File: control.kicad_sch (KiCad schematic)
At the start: 0 parts

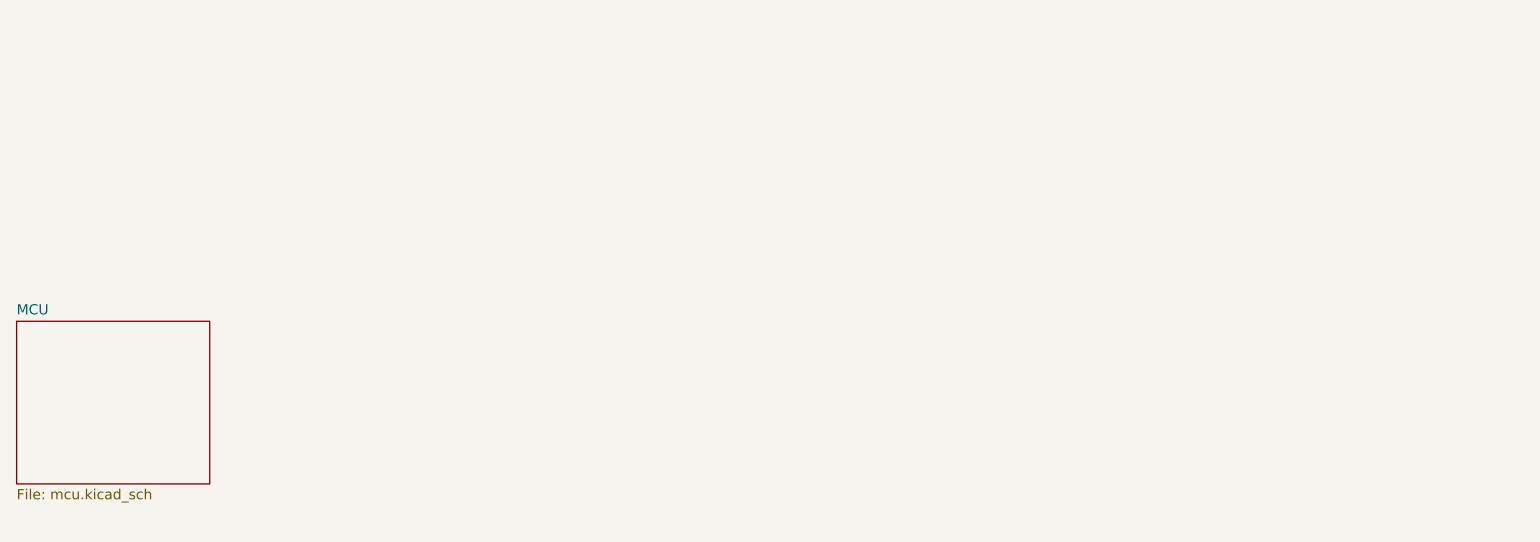
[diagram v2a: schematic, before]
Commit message: add MAX33071
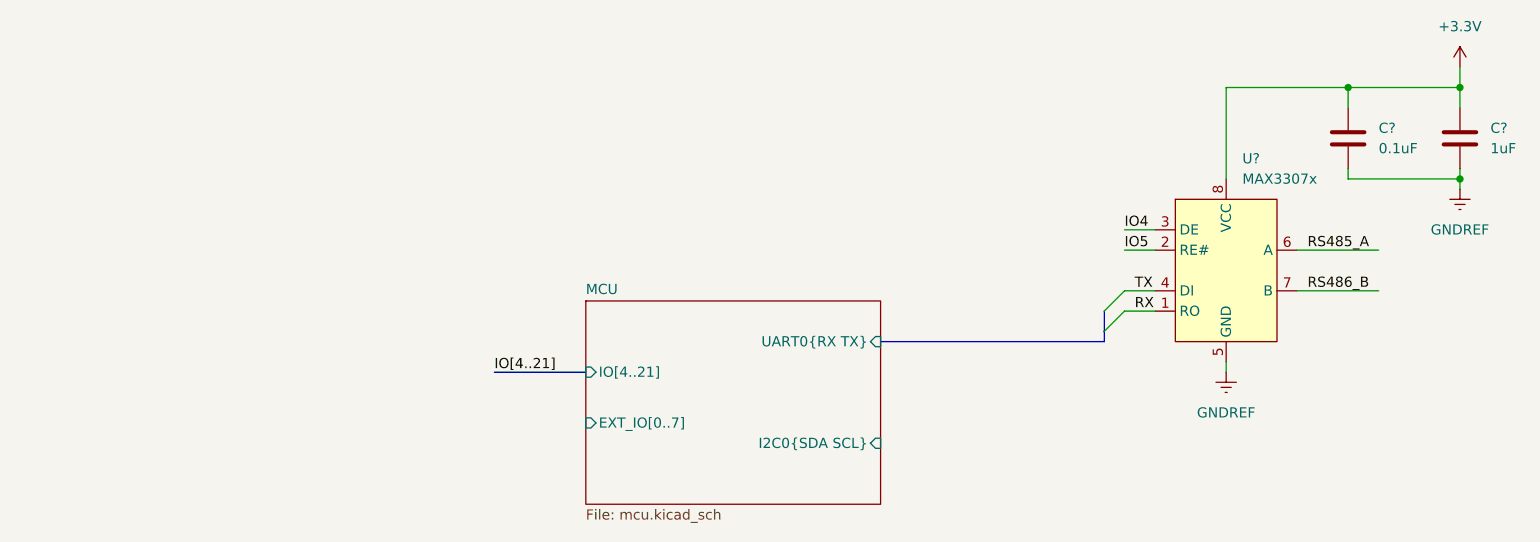
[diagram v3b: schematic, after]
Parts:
- added C?: 0.1uF, symbol Device:C
- added C?: 1uF, symbol Device:C
- added U?: MAX3307x, Package_SO:SO-8_3.9x4.9mm_P1.27mm, symbol Toadly:MAX3307x
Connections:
- new net +3.3V: C?.1, C?.1, U?.8 (VCC)
- new net GNDREF: C?.2, C?.2, U?.5 (GND)
- new net IO4: U?.3 (DE)
- new net IO5: U?.2 (RE#)
- new net RS485_A: U?.6 (A)
- new net RS486_B: U?.7 (B)
- new net RX: U?.1 (RO)
- new net TX: U?.4 (DI)
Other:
- sheet MCU ports: added EXT_IO[0..7], I2C0{SDA SCL}, IO[4..21], UART0{RX TX}; removed none
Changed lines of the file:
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@@
 (kicad_sch (version 20211123) (generator eeschema)
   (paper "A4")
-  (sheet (at 77.47 72.39) (size 24.13 20.32) (fields_autoplaced)
+  (junction (at 257.81 54.61) (diameter 0) (color 0 0 0 0)
+  )
+  (junction (at 257.81 43.18) (diameter 0) (color 0 0 0 0)
+  )
+  (junction (at 243.84 43.18) (diameter 0) (color 0 0 0 0)
+  )
+  (bus_entry (at 215.9 68.58) (size -2.54 2.54)
+    (stroke (width 0) (type default) (color 0 0 0 0))
+  )
+  (bus_entry (at 215.9 71.12) (size -2.54 2.54)
+    (stroke (width 0) (type default) (color 0 0 0 0))
+  )
+  (wire (pts (xy 215.9 68.58) (xy 219.71 68.58))
+    (stroke (width 0) (type default) (color 0 0 0 0))
+  )
+  (wire (pts (xy 215.9 63.5) (xy 219.71 63.5))
+    (stroke (width 0) (type default) (color 0 0 0 0))
+  )
+  (wire (pts (xy 257.81 43.18) (xy 257.81 45.72))
+    (stroke (width 0) (type default) (color 0 0 0 0))
+  )
+  (wire (pts (xy 257.81 40.64) (xy 257.81 43.18))
+    (stroke (width 0) (type default) (color 0 0 0 0))
+  )
+  (wire (pts (xy 243.84 43.18) (xy 243.84 45.72))
+    (stroke (width 0) (type default) (color 0 0 0 0))
+  )
+  (bus (pts (xy 213.36 73.66) (xy 213.36 74.93))
+    (stroke (width 0) (type default) (color 0 0 0 0))
+  )
+  (wire (pts (xy 243.84 53.34) (xy 243.84 54.61))
+    (stroke (width 0) (type default) (color 0 0 0 0))
+  )
+  (bus (pts (xy 185.42 74.93) (xy 213.36 74.93))
+    (stroke (width 0) (type default) (color 0 0 0 0))
+  )
+  (wire (pts (xy 257.81 54.61) (xy 257.81 55.88))
+    (stroke (width 0) (type default) (color 0 0 0 0))
+  )
+  (wire (pts (xy 243.84 43.18) (xy 257.81 43.18))
+    (stroke (width 0) (type default) (color 0 0 0 0))
+  )
+  (wire (pts (xy 237.49 63.5) (xy 247.65 63.5))
+    (stroke (width 0) (type default) (color 0 0 0 0))
+  )
+  (wire (pts (xy 237.49 68.58) (xy 247.65 68.58))
+    (stroke (width 0) (type default) (color 0 0 0 0))
+  )
+  (wire (pts (xy 228.6 77.47) (xy 228.6 78.74))
+    (stroke (width 0) (type default) (color 0 0 0 0))
+  )
+  (wire (pts (xy 257.81 53.34) (xy 257.81 54.61))
+    (stroke (width 0) (type default) (color 0 0 0 0))
+  )
+  (wire (pts (xy 243.84 54.61) (xy 257.81 54.61))
+    (stroke (width 0) (type default) (color 0 0 0 0))
+  )
+  (wire (pts (xy 228.6 43.18) (xy 243.84 43.18))
+    (stroke (width 0) (type default) (color 0 0 0 0))
+  )
+  (bus (pts (xy 213.36 71.12) (xy 213.36 73.66))
+    (stroke (width 0) (type default) (color 0 0 0 0))
+  )
+  (wire (pts (xy 215.9 60.96) (xy 219.71 60.96))
+    (stroke (width 0) (type default) (color 0 0 0 0))
+  )
+  (bus (pts (xy 137.16 78.74) (xy 148.59 78.74))
+    (stroke (width 0) (type default) (color 0 0 0 0))
+  )
+  (wire (pts (xy 228.6 54.61) (xy 228.6 43.18))
+    (stroke (width 0) (type default) (color 0 0 0 0))
+  )
+  (wire (pts (xy 215.9 71.12) (xy 219.71 71.12))
+    (stroke (width 0) (type default) (color 0 0 0 0))
+  )
+  (label "IO4" (at 215.9 60.96 0)
+    (effects (font (size 1.27 1.27)) (justify left bottom))
+  )
+  (label "RS486_B" (at 238.76 68.58 0)
+    (effects (font (size 1.27 1.27)) (justify left bottom))
+  )
+  (label "TX" (at 217.17 68.58 0)
+    (effects (font (size 1.27 1.27)) (justify left bottom))
+  )
+  (label "RX" (at 217.17 71.12 0)
+    (effects (font (size 1.27 1.27)) (justify left bottom))
+  )
+  (label "IO[4..21]" (at 137.16 78.74 0)
+    (effects (font (size 1.27 1.27)) (justify left bottom))
+  )
+  (label "IO5" (at 215.9 63.5 0)
+    (effects (font (size 1.27 1.27)) (justify left bottom))
+  )
+  (label "RS485_A" (at 238.76 63.5 0)
+    (effects (font (size 1.27 1.27)) (justify left bottom))
+  )
+  (symbol (lib_id "power:+3.3V") (at 257.81 40.64 0) (unit 1)
+    (in_bom yes) (on_board yes) (fields_autoplaced)
+    (property "Reference" "#PWR?" (id 0) (at 257.81 44.45 0)
+      (effects (font (size 1.27 1.27)) hide)
+    )
+    (property "Value" "+3.3V" (id 1) (at 257.81 35.56 0))
+    (property "Footprint" "" (id 2) (at 257.81 40.64 0)
+      (effects (font (size 1.27 1.27)) hide)
+    )
+    (property "Datasheet" "" (id 3) (at 257.81 40.64 0)
+      (effects (font (size 1.27 1.27)) hide)
+    )
+    (pin "1")
+  )
+  (symbol (lib_id "power:GNDREF") (at 257.81 55.88 0) (unit 1)
+    (in_bom yes) (on_board yes) (fields_autoplaced)
+    (property "Reference" "#PWR?" (id 0) (at 257.81 62.23 0)
+      (effects (font (size 1.27 1.27)) hide)
+    )
+    (property "Value" "GNDREF" (id 1) (at 257.81 60.96 0))
+    (property "Footprint" "" (id 2) (at 257.81 55.88 0)
+      (effects (font (size 1.27 1.27)) hide)
+    )
+    (property "Datasheet" "" (id 3) (at 257.81 55.88 0)
+      (effects (font (size 1.27 1.27)) hide)
+    )
+    (pin "1")
+  )
+  (symbol (lib_id "power:GNDREF") (at 228.6 78.74 0) (unit 1)
+    (in_bom yes) (on_board yes) (fields_autoplaced)
+    (property "Reference" "#PWR?" (id 0) (at 228.6 85.09 0)
+      (effects (font (size 1.27 1.27)) hide)
+    )
+    (property "Value" "GNDREF" (id 1) (at 228.6 83.82 0))
+    (property "Footprint" "" (id 2) (at 228.6 78.74 0)
+      (effects (font (size 1.27 1.27)) hide)
+    )
+    (property "Datasheet" "" (id 3) (at 228.6 78.74 0)
+      (effects (font (size 1.27 1.27)) hide)
+    )
+    (pin "1")
+  )
+  (symbol (lib_id "Toadly:MAX3307x") (at 228.6 66.04 0) (unit 1)
+    (in_bom yes) (on_board yes) (fields_autoplaced)
+    (property "Reference" "U?" (id 0) (at 230.6194 52.07 0)
+      (effects (font (size 1.27 1.27)) (justify left))
+    )
+    (property "Value" "MAX3307x" (id 1) (at 230.6194 54.61 0)
+      (effects (font (size 1.27 1.27)) (justify left))
+    )
+    (property "Footprint" "Package_SO:SO-8_3.9x4.9mm_P1.27mm" (id 2) (at 252.73 44.45 0)
+      (effects (font (size 1.27 1.27)) hide)
+    )
+    (property "Datasheet" "https://www.analog.com/media/en/technical-documentation/data-sheets/MAX33070E-MAX33074E.pdf" (id 3) (at 283.845 47.625 0)
+      (effects (font (size 1.27 1.27)) hide)
+    )
+    (pin "1")
+    (pin "2")
+    (pin "3")
+    (pin "4")
+    (pin "5")
+    (pin "6")
+    (pin "7")
+    (pin "8")
+  )
+  (symbol (lib_id "Device:C") (at 243.84 49.53 0) (unit 1)
+    (in_bom yes) (on_board yes) (fields_autoplaced)
+    (property "Reference" "C?" (id 0) (at 247.65 48.2599 0)
+      (effects (font (size 1.27 1.27)) (justify left))
+    )
+    (property "Value" "0.1uF" (id 1) (at 247.65 50.7999 0)
+      (effects (font (size 1.27 1.27)) (justify left))
+    )
+    (property "Footprint" "" (id 2) (at 244.8052 53.34 0)
+      (effects (font (size 1.27 1.27)) hide)
+    )
+    (property "Datasheet" "~" (id 3) (at 243.84 49.53 0)
+      (effects (font (size 1.27 1.27)) hide)
+    )
+    (pin "1")
+    (pin "2")
+  )
+  (symbol (lib_id "Device:C") (at 257.81 49.53 0) (unit 1)
+    (in_bom yes) (on_board yes) (fields_autoplaced)
+    (property "Reference" "C?" (id 0) (at 261.62 48.2599 0)
+      (effects (font (size 1.27 1.27)) (justify left))
+    )
+    (property "Value" "1uF" (id 1) (at 261.62 50.7999 0)
+      (effects (font (size 1.27 1.27)) (justify left))
+    )
+    (property "Footprint" "" (id 2) (at 258.7752 53.34 0)
+      (effects (font (size 1.27 1.27)) hide)
+    )
+    (property "Datasheet" "~" (id 3) (at 257.81 49.53 0)
+      (effects (font (size 1.27 1.27)) hide)
+    )
+    (pin "1")
+    (pin "2")
+  )
+  (sheet (at 148.59 69.85) (size 36.83 25.4) (fields_autoplaced)
     (stroke (width 0.1524) (type solid) (color 0 0 0 0))
     (fill (color 255 242 138 1.0000))
-    (property "Sheet name" "MCU" (id 0) (at 77.47 71.6784 0)
+    (property "Sheet name" "MCU" (id 0) (at 148.59 69.1384 0)
       (effects (font (size 1.27 1.27)) (justify left bottom))
     )
-    (property "Sheet file" "mcu.kicad_sch" (id 1) (at 77.47 93.2946 0)
+    (property "Sheet file" "mcu.kicad_sch" (id 1) (at 148.59 95.8346 0)
       (effects (font (size 1.27 1.27)) (justify left top))
+    )
+    (pin "IO[4..21]" input (at 148.59 78.74 180)
+      (effects (font (size 1.27 1.27)) (justify left))
+    )
+    (pin "EXT_IO[0..7]" input (at 148.59 85.09 180)
+      (effects (font (size 1.27 1.27)) (justify left))
+    )
+    (pin "UART0{RX TX}" input (at 185.42 74.93 0)
+      (effects (font (size 1.27 1.27)) (justify right))
+    )
+    (pin "I2C0{SDA SCL}" input (at 185.42 87.63 0)
+      (effects (font (size 1.27 1.27)) (justify right))
     )
   )
@@
   )
   (symbol_instances
+    (path "/15a68dc8-3451-494e-bad4-ff2f83dea659"
+      (reference "#PWR?") (unit 1) (value "+3.3V") (footprint "")
+    )
+    (path "/182c1680-7ab1-4148-afbd-7669f42983bc"
+      (reference "#PWR?") (unit 1) (value "GNDREF") (footprint "")
+    )
+    (path "/1b1655f0-b4d0-4eaf-895a-1e15754c5ef0"
+      (reference "#PWR?") (unit 1) (value "GNDREF") (footprint "")
+    )
     (path "/07551e16-8169-4161-b345-aacecb867638/29f85bc4-5366-44e4-82af-f2b0426f74d8"
       (reference "#PWR?") (unit 1) (value "GNDREF") (footprint "")
@@
       (reference "C?") (unit 1) (value "0.1uF") (footprint "Capacitor_SMD:C_0805_2012Metric_Pad1.18x1.45mm_HandSolder")
     )
+    (path "/d082b342-8f66-4176-9074-d53604146507"
+      (reference "C?") (unit 1) (value "0.1uF") (footprint "")
+    )
+    (path "/e329f5dd-ac54-4ef4-a779-6352db7141e0"
+      (reference "C?") (unit 1) (value "1uF") (footprint "")
+    )
     (path "/07551e16-8169-4161-b345-aacecb867638/9b6bb144-9793-4a93-9062-c00790b7e790"
       (reference "R?") (unit 1) (value "DNP") (footprint "Resistor_SMD:R_0805_2012Metric_Pad1.20x1.40mm_HandSolder")
@@
       (reference "R?") (unit 1) (value "DNP") (footprint "Resistor_SMD:R_0805_2012Metric_Pad1.20x1.40mm_HandSolder")
     )
+    (path "/787cb8e8-89e7-45c4-a31d-b183c4f10785"
+      (reference "U?") (unit 1) (value "MAX3307x") (footprint "Package_SO:SO-8_3.9x4.9mm_P1.27mm")
+    )
     (path "/07551e16-8169-4161-b345-aacecb867638/c77ac548-f949-486b-8a0a-c0173407b5bf"

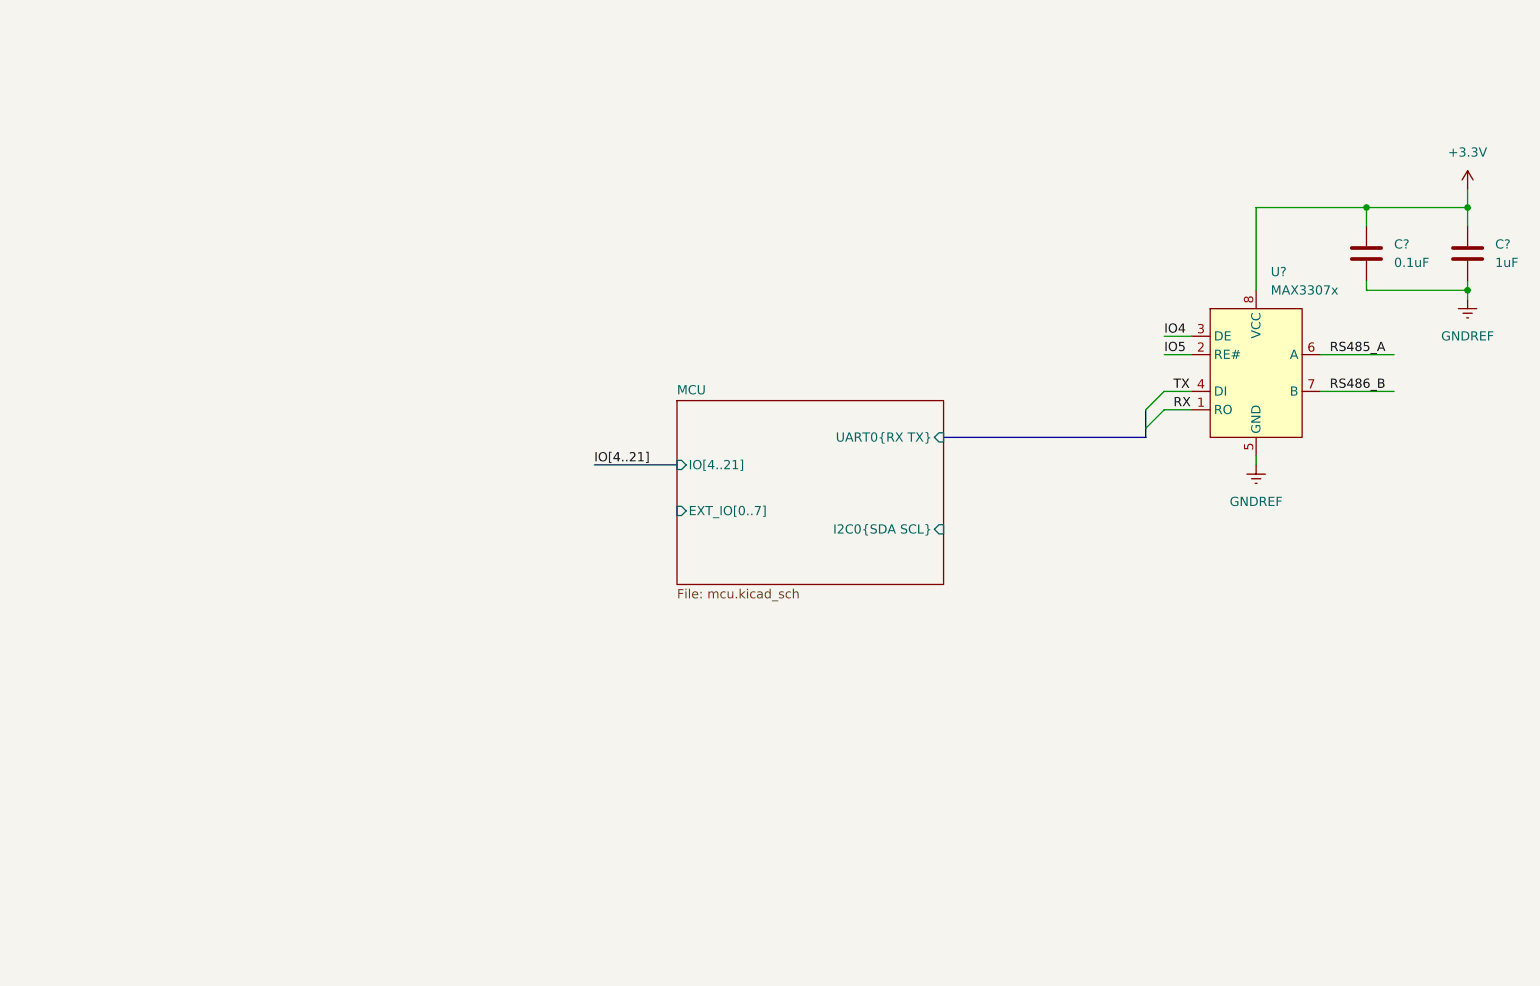
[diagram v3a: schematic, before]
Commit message: add 40pin IDC connector
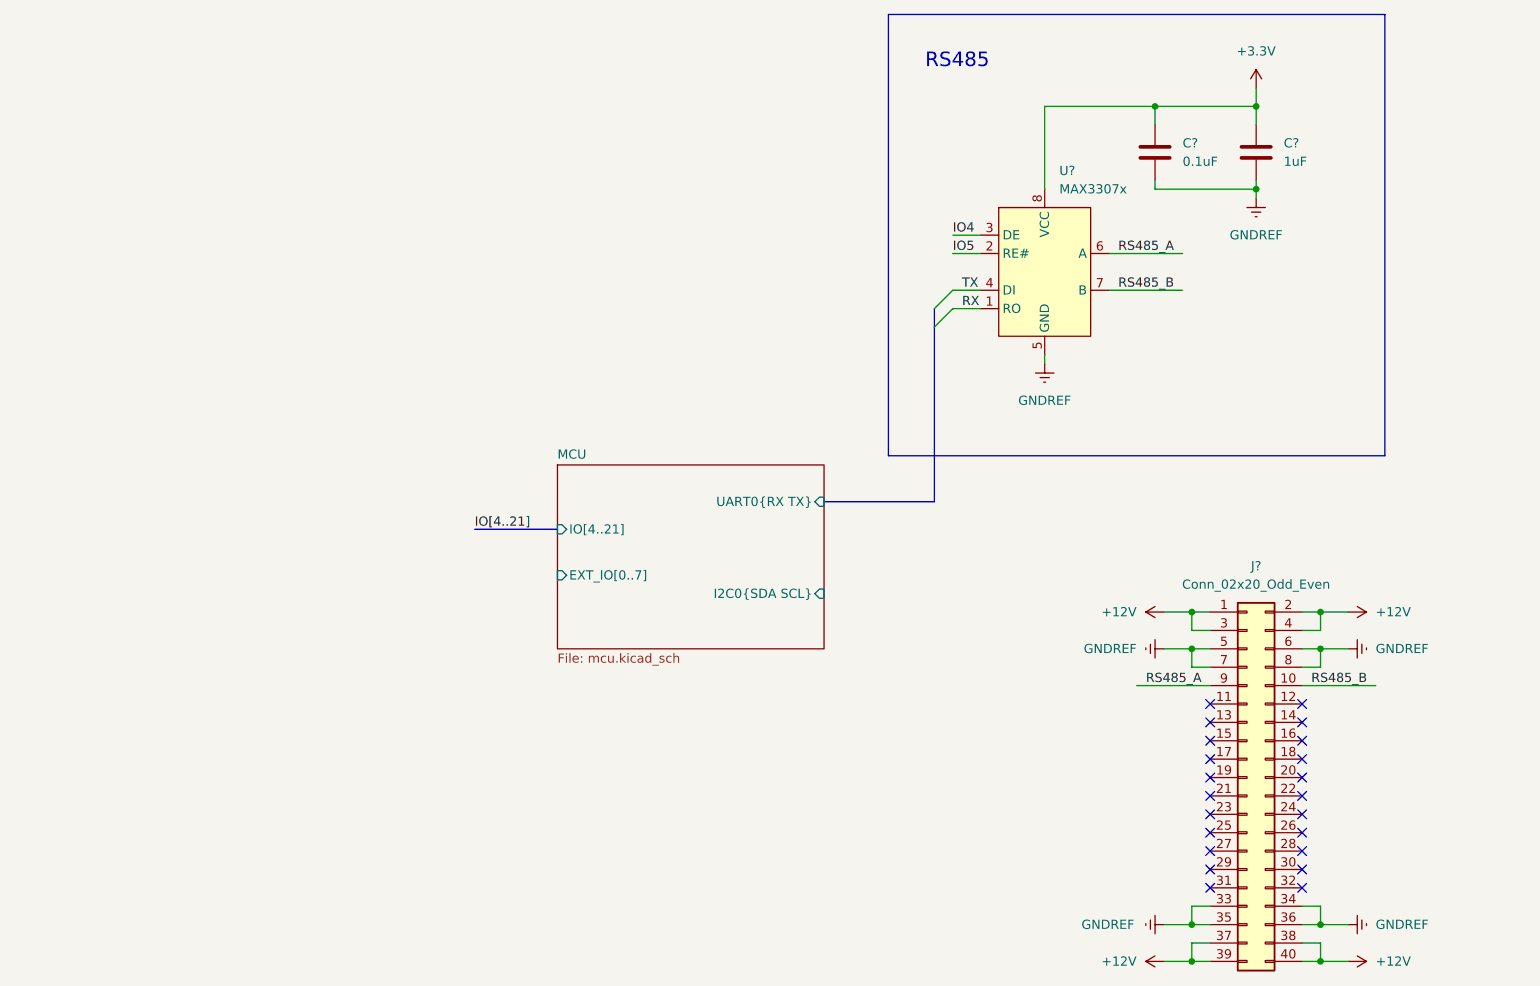
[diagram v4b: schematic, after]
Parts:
- added J?: Conn_02x20_Odd_Even, symbol Connector_Generic:Conn_02x20_Odd_Even
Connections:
- net GNDREF: now also J?.33 (Pin_33), J?.34 (Pin_34), J?.35 (Pin_35), J?.36 (Pin_36), J?.5 (Pin_5), J?.6 (Pin_6), J?.7 (Pin_7), J?.8 (Pin_8)
- net RS485_A: now also J?.9 (Pin_9)
- net RS486_B renamed RS485_B
- net RS485_B: now also J?.10 (Pin_10)
- new net +12V: J?.1 (Pin_1), J?.2 (Pin_2), J?.3 (Pin_3), J?.37 (Pin_37), J?.38 (Pin_38), J?.39 (Pin_39), J?.4 (Pin_4), J?.40 (Pin_40)
- no-connect marks 0 -> 22
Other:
- note added: "RS485"
- moved on the sheet: C?, U?

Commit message: add IO page and flood light drivers
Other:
- added sheet IO (io.kicad_sch)

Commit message: rename IO to Drivers
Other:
- sheet IO renamed Drivers
- sheet Drivers: file io.kicad_sch -> drivers.kicad_sch
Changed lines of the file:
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@@
     (stroke (width 0.1524) (type solid) (color 0 0 0 0))
     (fill (color 255 242 138 1.0000))
-    (property "Sheet name" "IO" (id 0) (at 57.15 69.1384 0)
+    (property "Sheet name" "Drivers" (id 0) (at 57.15 69.1384 0)
       (effects (font (size 1.27 1.27)) (justify left bottom))
     )
-    (property "Sheet file" "io.kicad_sch" (id 1) (at 57.15 112.3446 0)
+    (property "Sheet file" "drivers.kicad_sch" (id 1) (at 57.15 112.3446 0)
       (effects (font (size 1.27 1.27)) (justify left top))
     )
